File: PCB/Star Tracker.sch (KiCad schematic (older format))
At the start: 24 parts

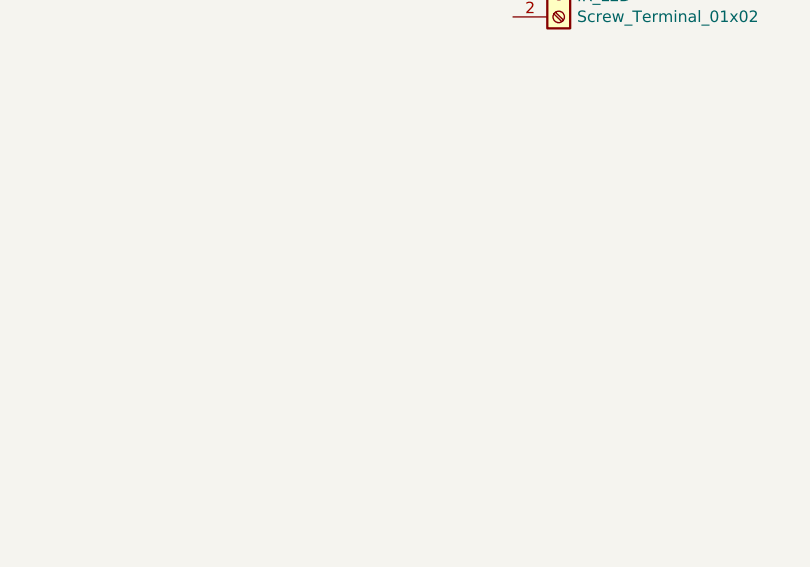
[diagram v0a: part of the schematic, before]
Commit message: Added status LEDs
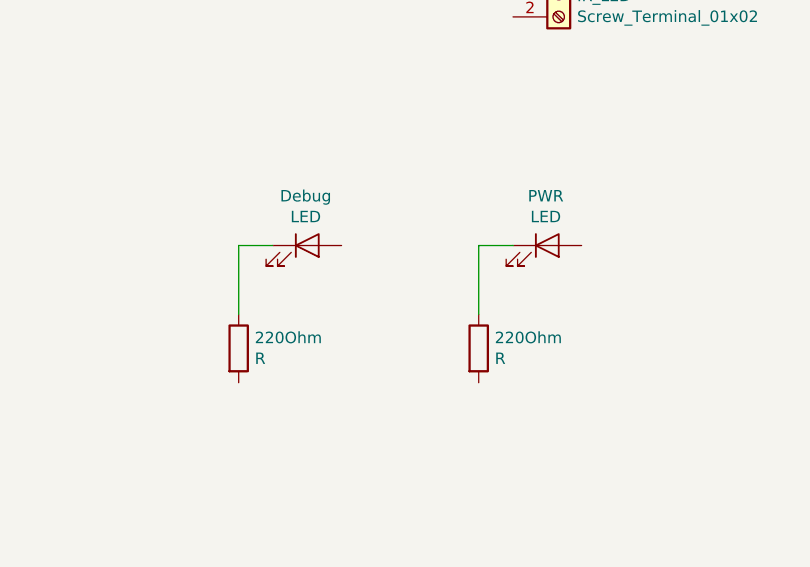
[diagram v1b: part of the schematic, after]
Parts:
- added 220Ohm (x2): R, symbol Device:R
- added Debug, PWR: LED, symbol Device:LED
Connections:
- new net: 220Ohm.1, PWR.1 (K)
- new net: 220Ohm.1, Debug.1 (K)
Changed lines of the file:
@@
 EESchema Schematic File Version 4
 LIBS:power
+LIBS:device
 LIBS:74xx
+LIBS:audio
+LIBS:interface
+LIBS:Star Tracker-cache
 EELAYER 30 0
 EELAYER END
@@
 	1    0    0    -1
 $EndComp
+$Comp
+L Device:LED PWR
+U 1 1 5D8AF065
+P 9850 4800
+F 0 "PWR" H 9843 5016 50  0000 C CNN
+F 1 "LED" H 9843 4925 50  0000 C CNN
+F 2 "" H 9850 4800 50  0001 C CNN
+F 3 "~" H 9850 4800 50  0001 C CNN
+	1    9850 4800
+	1    0    0    -1
+$EndComp
+$Comp
+L Device:LED Debug
+U 1 1 5D8B0AB5
+P 8800 4800
+F 0 "Debug" H 8793 5016 50  0000 C CNN
+F 1 "LED" H 8793 4925 50  0000 C CNN
+F 2 "" H 8800 4800 50  0001 C CNN
+F 3 "~" H 8800 4800 50  0001 C CNN
+	1    8800 4800
+	1    0    0    -1
+$EndComp
+$Comp
+L Device:R 220Ohm
+U 1 1 5D8B33E6
+P 8500 5250
+F 0 "220Ohm" H 8570 5296 50  0000 L CNN
+F 1 "R" H 8570 5205 50  0000 L CNN
+F 2 "" V 8430 5250 50  0001 C CNN
+F 3 "~" H 8500 5250 50  0001 C CNN
+	1    8500 5250
+	1    0    0    -1
+$EndComp
+$Comp
+L Device:R 220Ohm
+U 1 1 5D8B3CED
+P 9550 5250
+F 0 "220Ohm" H 9620 5296 50  0000 L CNN
+F 1 "R" H 9620 5205 50  0000 L CNN
+F 2 "" V 9480 5250 50  0001 C CNN
+F 3 "~" H 9550 5250 50  0001 C CNN
+	1    9550 5250
+	1    0    0    -1
+$EndComp
+Wire Wire Line
+	9700 4800 9550 4800
+Wire Wire Line
+	9550 4800 9550 5100
+Wire Wire Line
+	8650 4800 8500 4800
+Wire Wire Line
+	8500 4800 8500 5100
 $EndSCHEMATC

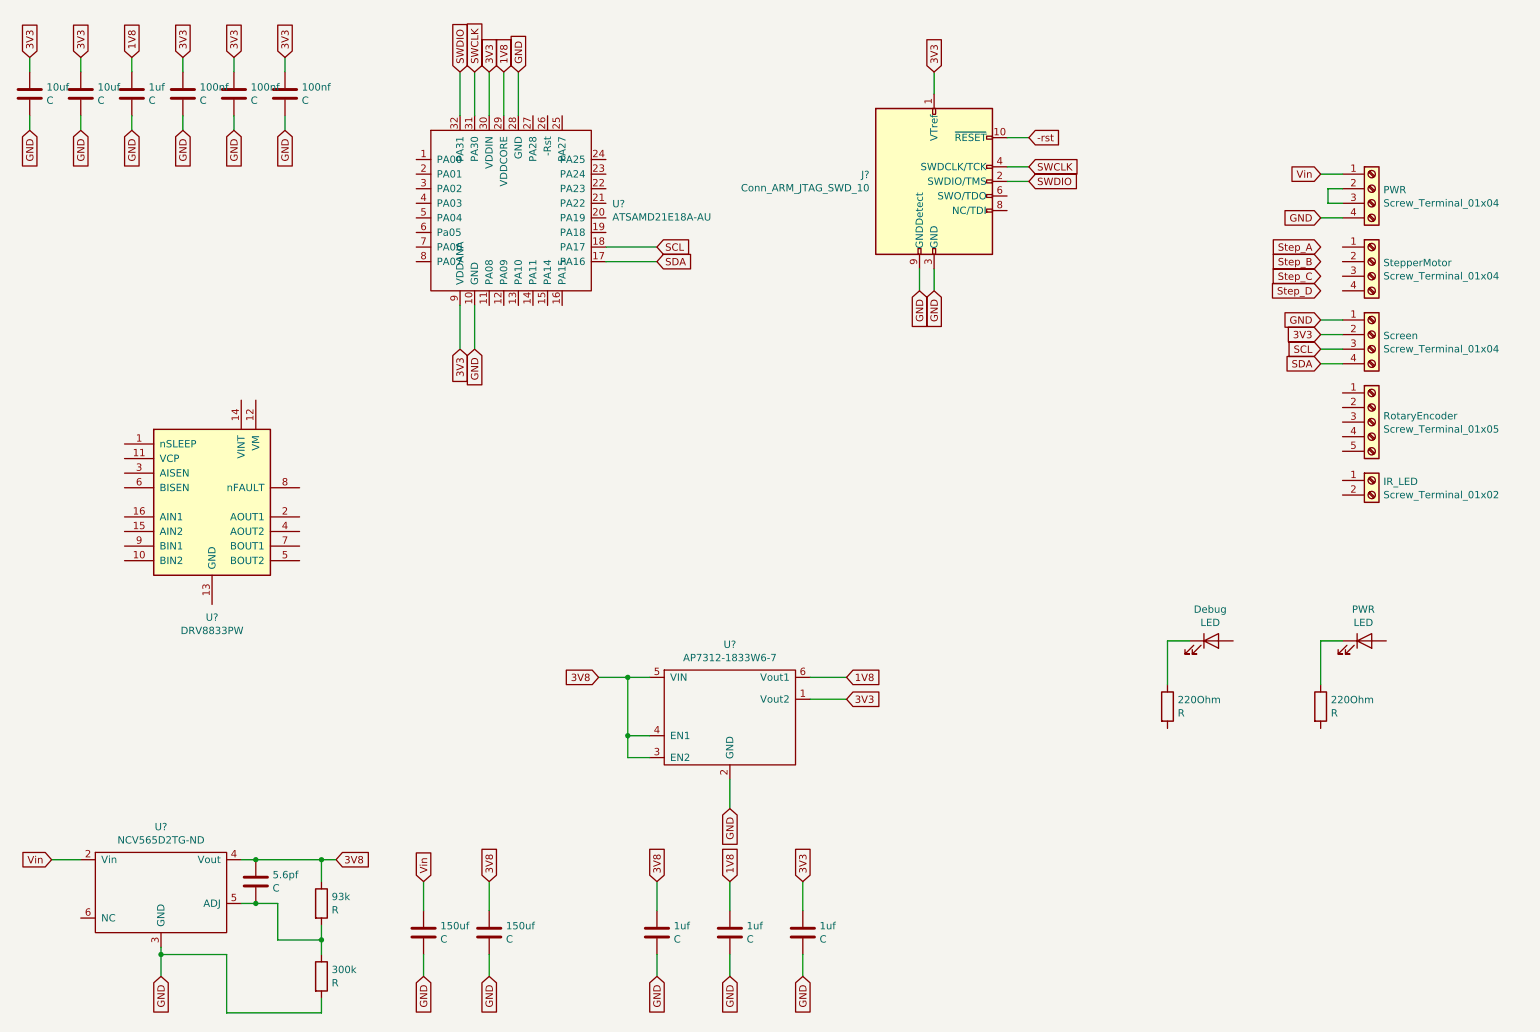
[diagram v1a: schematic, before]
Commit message: Connected some more screw terminals
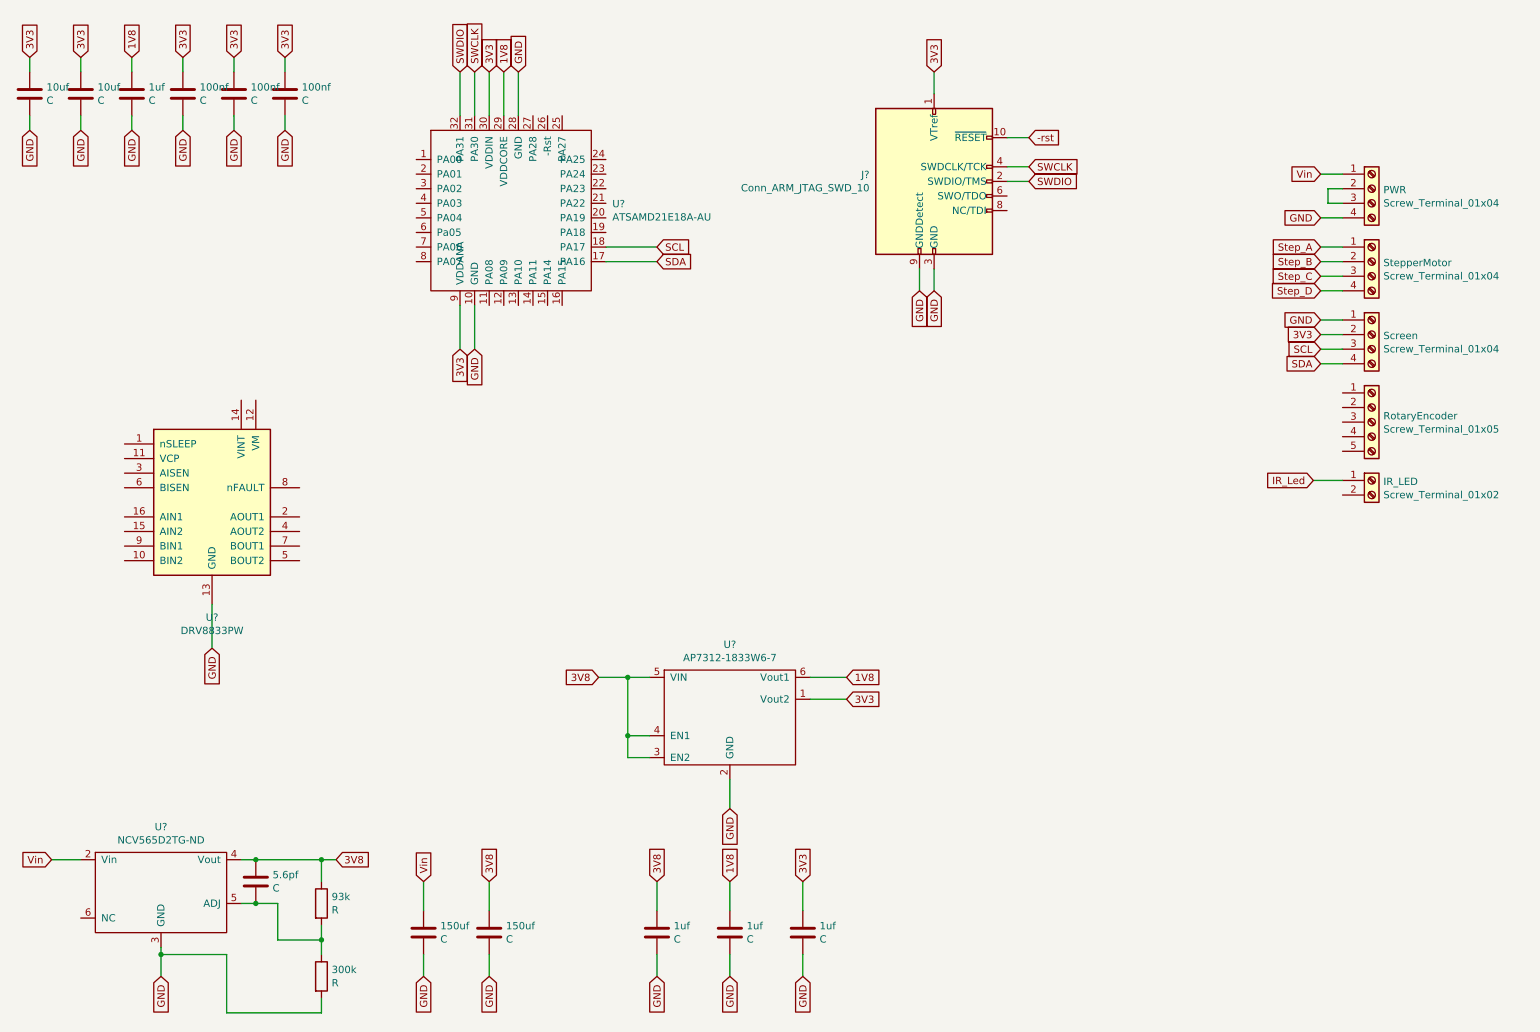
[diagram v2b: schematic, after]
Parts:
- removed 220Ohm (x2): R, symbol Device:R
- removed Debug, PWR: LED, symbol Device:LED
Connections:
- net GND: now also U?.13 (GND)
- net Step_A: now also StepperMotor.1 (Pin_1)
- net Step_B: now also StepperMotor.2 (Pin_2)
- net Step_C: now also StepperMotor.3 (Pin_3)
- net Step_D: now also StepperMotor.4 (Pin_4)
- net IR_Led: now reaches IR_LED.1 (Pin_1)
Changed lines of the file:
@@
 EESchema Schematic File Version 4
-LIBS:power
-LIBS:device
-LIBS:74xx
-LIBS:audio
-LIBS:interface
-LIBS:Star Tracker-cache
 EELAYER 30 0
 EELAYER END
@@
 	1    0    0    -1
 $EndComp
-$Comp
-L Device:LED PWR
-U 1 1 5D8AF065
-P 9850 4800
-F 0 "PWR" H 9843 5016 50  0000 C CNN
-F 1 "LED" H 9843 4925 50  0000 C CNN
-F 2 "" H 9850 4800 50  0001 C CNN
-F 3 "~" H 9850 4800 50  0001 C CNN
-	1    9850 4800
-	1    0    0    -1
-$EndComp
-$Comp
-L Device:LED Debug
-U 1 1 5D8B0AB5
-P 8800 4800
-F 0 "Debug" H 8793 5016 50  0000 C CNN
-F 1 "LED" H 8793 4925 50  0000 C CNN
-F 2 "" H 8800 4800 50  0001 C CNN
-F 3 "~" H 8800 4800 50  0001 C CNN
-	1    8800 4800
-	1    0    0    -1
-$EndComp
-$Comp
-L Device:R 220Ohm
-U 1 1 5D8B33E6
-P 8500 5250
-F 0 "220Ohm" H 8570 5296 50  0000 L CNN
-F 1 "R" H 8570 5205 50  0000 L CNN
-F 2 "" V 8430 5250 50  0001 C CNN
-F 3 "~" H 8500 5250 50  0001 C CNN
-	1    8500 5250
-	1    0    0    -1
-$EndComp
-$Comp
-L Device:R 220Ohm
-U 1 1 5D8B3CED
-P 9550 5250
-F 0 "220Ohm" H 9620 5296 50  0000 L CNN
-F 1 "R" H 9620 5205 50  0000 L CNN
-F 2 "" V 9480 5250 50  0001 C CNN
-F 3 "~" H 9550 5250 50  0001 C CNN
-	1    9550 5250
-	1    0    0    -1
-$EndComp
-Wire Wire Line
-	9700 4800 9550 4800
-Wire Wire Line
-	9550 4800 9550 5100
-Wire Wire Line
-	8650 4800 8500 4800
-Wire Wire Line
-	8500 4800 8500 5100
+Text GLabel 9500 3700 0    50   Input ~ 0
+IR_Led
+Wire Wire Line
+	9500 3700 9700 3700
+Wire Wire Line
+	9550 2100 9700 2100
+Wire Wire Line
+	9700 2200 9550 2200
+Wire Wire Line
+	9550 2300 9700 2300
+Wire Wire Line
+	9700 2400 9550 2400
+Text GLabel 1950 4850 3    50   Input ~ 0
+GND
+Wire Wire Line
+	1950 4550 1950 4850
 $EndSCHEMATC

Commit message: Finished first pass at schematic
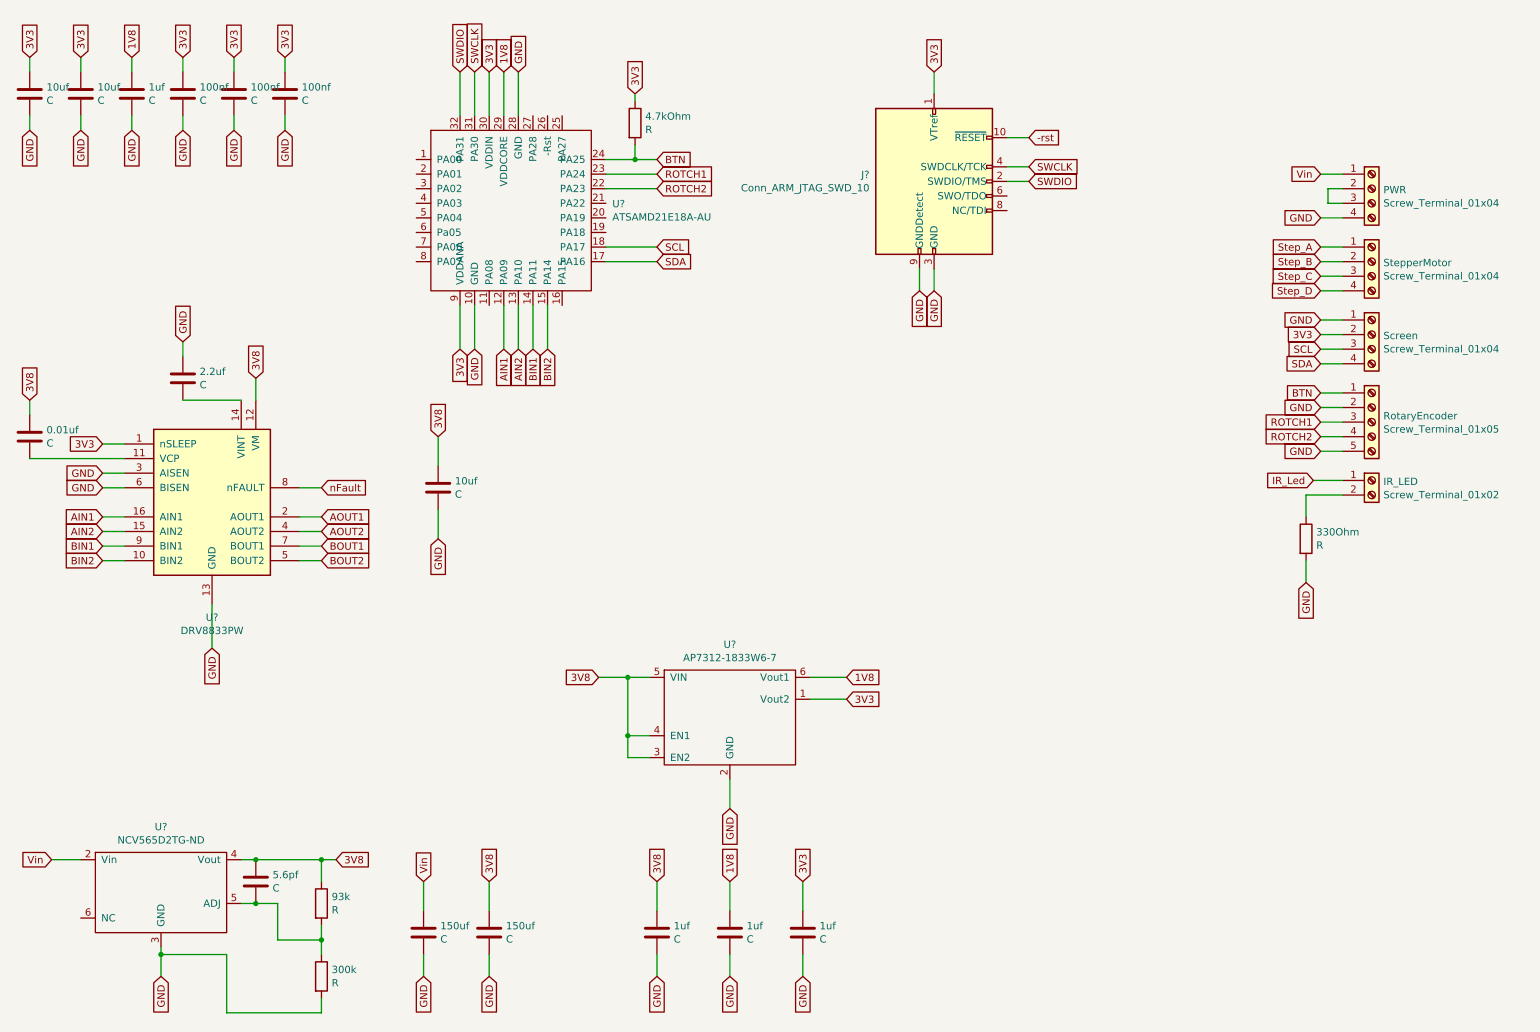
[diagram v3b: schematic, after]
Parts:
- added 0.01uf, 10uf, 2.2uf: C, symbol Device:C
- added 330Ohm, 4.7kOhm: R, symbol Device:R
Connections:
- net 3V3: now also U?.1 (nSLEEP), 4.7kOhm.1
- net 3V8: now also U?.12 (VM), 0.01uf.1, 10uf.1
- net GND: now also RotaryEncoder.2 (Pin_2), RotaryEncoder.5 (Pin_5), U?.3 (AISEN), U?.6 (BISEN), 10uf.2, 2.2uf.1, 330Ohm.2
- net AIN1: now reaches U?.12 (PA09)
- net AIN1: now also U?.16 (AIN1)
- net AIN2: now reaches U?.13 (PA10)
- net AIN2: now also U?.15 (AIN2)
- net BIN1: now reaches U?.14 (PA11)
- net BIN1: now also U?.9 (BIN1)
- net BIN2: now reaches U?.15 (PA14)
- net BIN2: now also U?.10 (BIN2)
- net ROTCH2: now reaches U?.22 (PA23)
- net ROTCH2: now also RotaryEncoder.4 (Pin_4)
- net ROTCH1: now reaches U?.23 (PA24)
- net ROTCH1: now also RotaryEncoder.3 (Pin_3)
- net BTN: now reaches U?.24 (PA25)
- net BTN: now also RotaryEncoder.1 (Pin_1), 4.7kOhm.2
- net at U?.11 (VCP): now also 0.01uf.2
- net at U?.14 (VINT): now also 2.2uf.2
- net AOUT1: now reaches U?.2 (AOUT1)
- net AOUT2: now reaches U?.4 (AOUT2)
- net BOUT2: now reaches U?.5 (BOUT2)
- net BOUT1: now reaches U?.7 (BOUT1)
- net nFault: now reaches U?.8 (nFAULT)
- net at IR_LED.2 (Pin_2): now also 330Ohm.1
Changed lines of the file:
@@
 EESchema Schematic File Version 4
+LIBS:power
+LIBS:device
+LIBS:74xx
+LIBS:audio
+LIBS:interface
+LIBS:Star Tracker-cache
 EELAYER 30 0
 EELAYER END
@@
 Wire Wire Line
 	1950 4550 1950 4850
+Text GLabel 2700 3950 2    50   Input ~ 0
+AOUT1
+Text GLabel 2700 4050 2    50   Input ~ 0
+AOUT2
+Text GLabel 2700 4150 2    50   Input ~ 0
+BOUT1
+Text GLabel 2700 4250 2    50   Input ~ 0
+BOUT2
+Text GLabel 1200 3950 0    50   Input ~ 0
+AIN1
+Text GLabel 1200 4050 0    50   Input ~ 0
+AIN2
+Text GLabel 1200 4150 0    50   Input ~ 0
+BIN1
+Text GLabel 1200 4250 0    50   Input ~ 0
+BIN2
+Wire Wire Line
+	1200 3950 1350 3950
+Wire Wire Line
+	1200 4050 1350 4050
+Wire Wire Line
+	1200 4150 1350 4150
+Wire Wire Line
+	1200 4250 1350 4250
+Wire Wire Line
+	2550 3950 2700 3950
+Wire Wire Line
+	2550 4050 2700 4050
+Wire Wire Line
+	2550 4150 2700 4150
+Wire Wire Line
+	2550 4250 2700 4250
+Text GLabel 1200 3650 0    50   Input ~ 0
+GND
+Text GLabel 1200 3750 0    50   Input ~ 0
+GND
+Wire Wire Line
+	1200 3650 1350 3650
+Wire Wire Line
+	1200 3750 1350 3750
+Text GLabel 2250 3000 1    50   Input ~ 0
+3V8
+Text GLabel 1200 3450 0    50   Input ~ 0
+3V3
+Text GLabel 700  3150 1    50   Input ~ 0
+3V8
+Text GLabel 1750 2750 1    50   Input ~ 0
+GND
+$Comp
+L Device:C 0.01uf
+U 1 1 5D954C46
+P 700 3400
+F 0 "0.01uf" H 815 3446 50  0000 L CNN
+F 1 "C" H 815 3355 50  0000 L CNN
+F 2 "" H 738 3250 50  0001 C CNN
+F 3 "~" H 700 3400 50  0001 C CNN
+	1    700  3400
+	1    0    0    -1
+$EndComp
+$Comp
+L Device:C 2.2uf
+U 1 1 5D95571D
+P 1750 3000
+F 0 "2.2uf" H 1865 3046 50  0000 L CNN
+F 1 "C" H 1865 2955 50  0000 L CNN
+F 2 "" H 1788 2850 50  0001 C CNN
+F 3 "~" H 1750 3000 50  0001 C CNN
+	1    1750 3000
+	1    0    0    -1
+$EndComp
+$Comp
+L Device:C 10uf
+U 1 1 5D955D2C
+P 3500 3750
+F 0 "10uf" H 3615 3796 50  0000 L CNN
+F 1 "C" H 3615 3705 50  0000 L CNN
+F 2 "" H 3538 3600 50  0001 C CNN
+F 3 "~" H 3500 3750 50  0001 C CNN
+	1    3500 3750
+	1    0    0    -1
+$EndComp
+Wire Wire Line
+	700  3150 700  3250
+Wire Wire Line
+	700  3550 1350 3550
+Wire Wire Line
+	1750 2750 1750 2850
+Wire Wire Line
+	1750 3150 2150 3150
+Wire Wire Line
+	2250 3000 2250 3150
+Wire Wire Line
+	1200 3450 1350 3450
+Text GLabel 3500 3400 1    50   Input ~ 0
+3V8
+Text GLabel 3500 4100 3    50   Input ~ 0
+GND
+Wire Wire Line
+	3500 3400 3500 3600
+Wire Wire Line
+	3500 3900 3500 4100
+Text GLabel 2700 3750 2    50   Input ~ 0
+nFault
+Wire Wire Line
+	2550 3750 2700 3750
+$Comp
+L Device:R 330Ohm
+U 1 1 5D96EC16
+P 9450 4100
+F 0 "330Ohm" H 9520 4146 50  0000 L CNN
+F 1 "R" H 9520 4055 50  0000 L CNN
+F 2 "" V 9380 4100 50  0001 C CNN
+F 3 "~" H 9450 4100 50  0001 C CNN
+	1    9450 4100
+	1    0    0    -1
+$EndComp
+Text GLabel 9450 4400 3    50   Input ~ 0
+GND
+Wire Wire Line
+	9700 3800 9450 3800
+Wire Wire Line
+	9450 3800 9450 3950
+Wire Wire Line
+	9450 4250 9450 4400
+Text GLabel 9550 3100 0    50   Input ~ 0
+BTN
+Text GLabel 9550 3300 0    50   Input ~ 0
+ROTCH1
+Text GLabel 9550 3400 0    50   Input ~ 0
+ROTCH2
+Text GLabel 9550 3500 0    50   Input ~ 0
+GND
+Text GLabel 9550 3200 0    50   Input ~ 0
+GND
+Wire Wire Line
+	9550 3100 9700 3100
+Wire Wire Line
+	9700 3200 9550 3200
+Wire Wire Line
+	9550 3300 9700 3300
+Wire Wire Line
+	9700 3400 9550 3400
+Wire Wire Line
+	9700 3500 9550 3500
+Text GLabel 5000 1500 2    50   Input ~ 0
+BTN
+Text GLabel 4850 1050 1    50   Input ~ 0
+3V3
+$Comp
+L Device:R 4.7kOhm
+U 1 1 5D99025B
+P 4850 1250
+F 0 "4.7kOhm" H 4920 1296 50  0000 L CNN
+F 1 "R" H 4920 1205 50  0000 L CNN
+F 2 "" V 4780 1250 50  0001 C CNN
+F 3 "~" H 4850 1250 50  0001 C CNN
+	1    4850 1250
+	1    0    0    -1
+$EndComp
+Wire Wire Line
+	4850 1050 4850 1100
+Wire Wire Line
+	4850 1400 4850 1500
+Wire Wire Line
+	4850 1500 5000 1500
+Wire Wire Line
+	4850 1500 4650 1500
+Connection ~ 4850 1500
+Text GLabel 5000 1600 2    50   Input ~ 0
+ROTCH1
+Text GLabel 5000 1700 2    50   Input ~ 0
+ROTCH2
+Text GLabel 3950 2800 3    50   Input ~ 0
+AIN1
+Text GLabel 4050 2800 3    50   Input ~ 0
+AIN2
+Text GLabel 4150 2800 3    50   Input ~ 0
+BIN1
+Text GLabel 4250 2800 3    50   Input ~ 0
+BIN2
+Wire Wire Line
+	3950 2800 3950 2500
+Wire Wire Line
+	4050 2800 4050 2500
+Wire Wire Line
+	4150 2800 4150 2500
+Wire Wire Line
+	4250 2800 4250 2500
+Wire Wire Line
+	5000 1600 4650 1600
+Wire Wire Line
+	5000 1700 4650 1700
 $EndSCHEMATC
